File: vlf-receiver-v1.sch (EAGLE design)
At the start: 46 parts, among them P10 10k, Q1 BC237A/EQUIV, Q2 BC237A/EQUIV, U1 MC7809, U2 TLE2426, U3 LM386

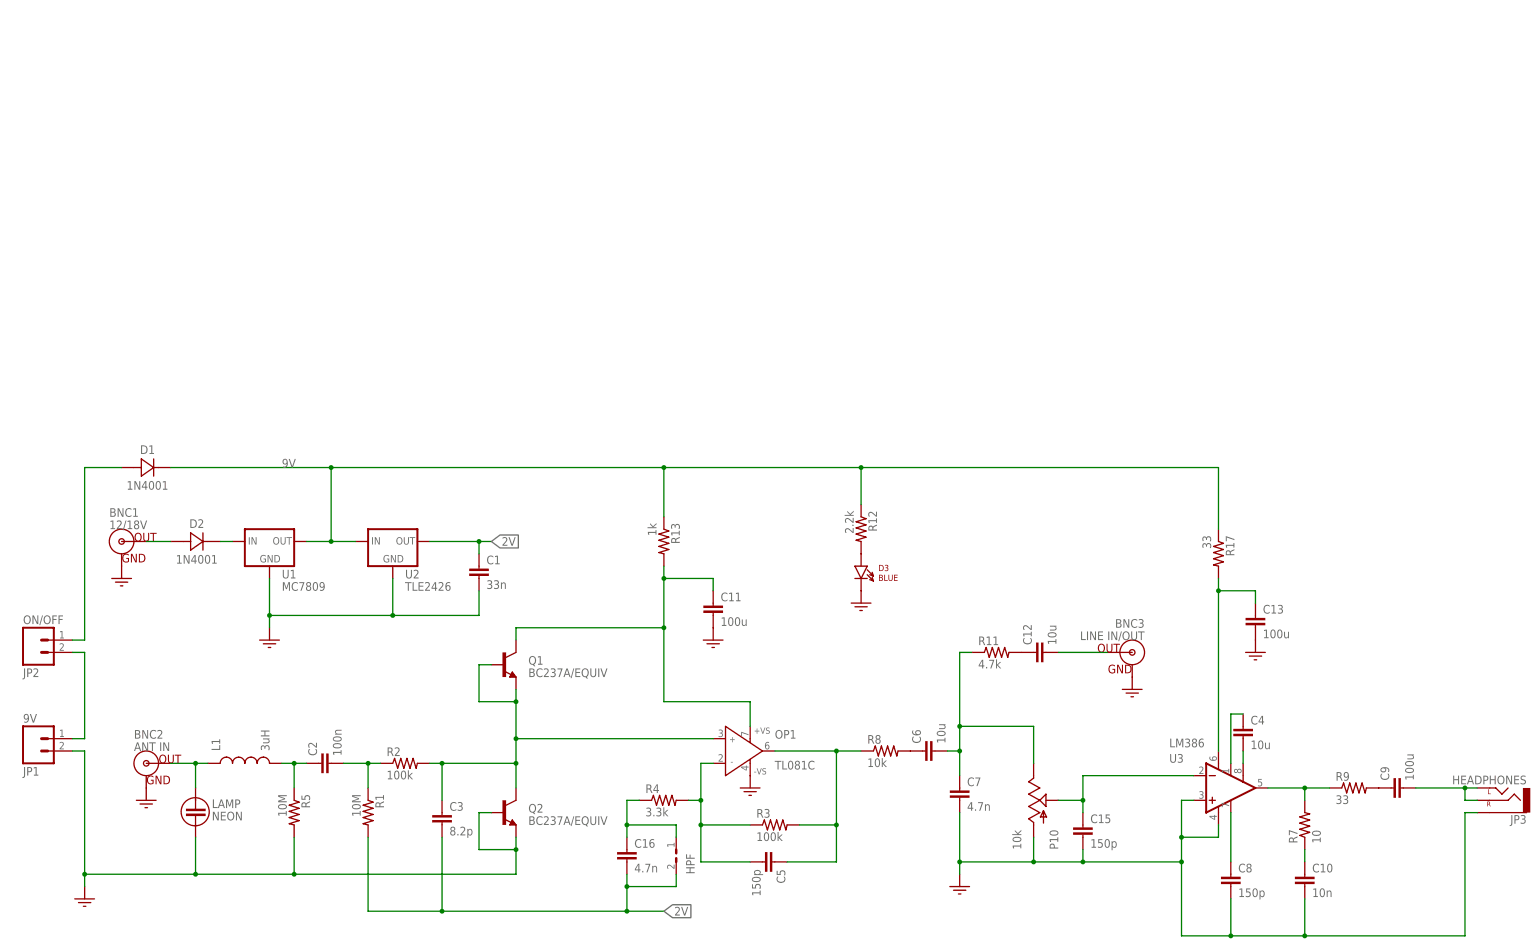
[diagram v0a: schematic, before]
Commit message: Changed name. Cleaned up schematic. Added notes and exported BOM. Need to compare.
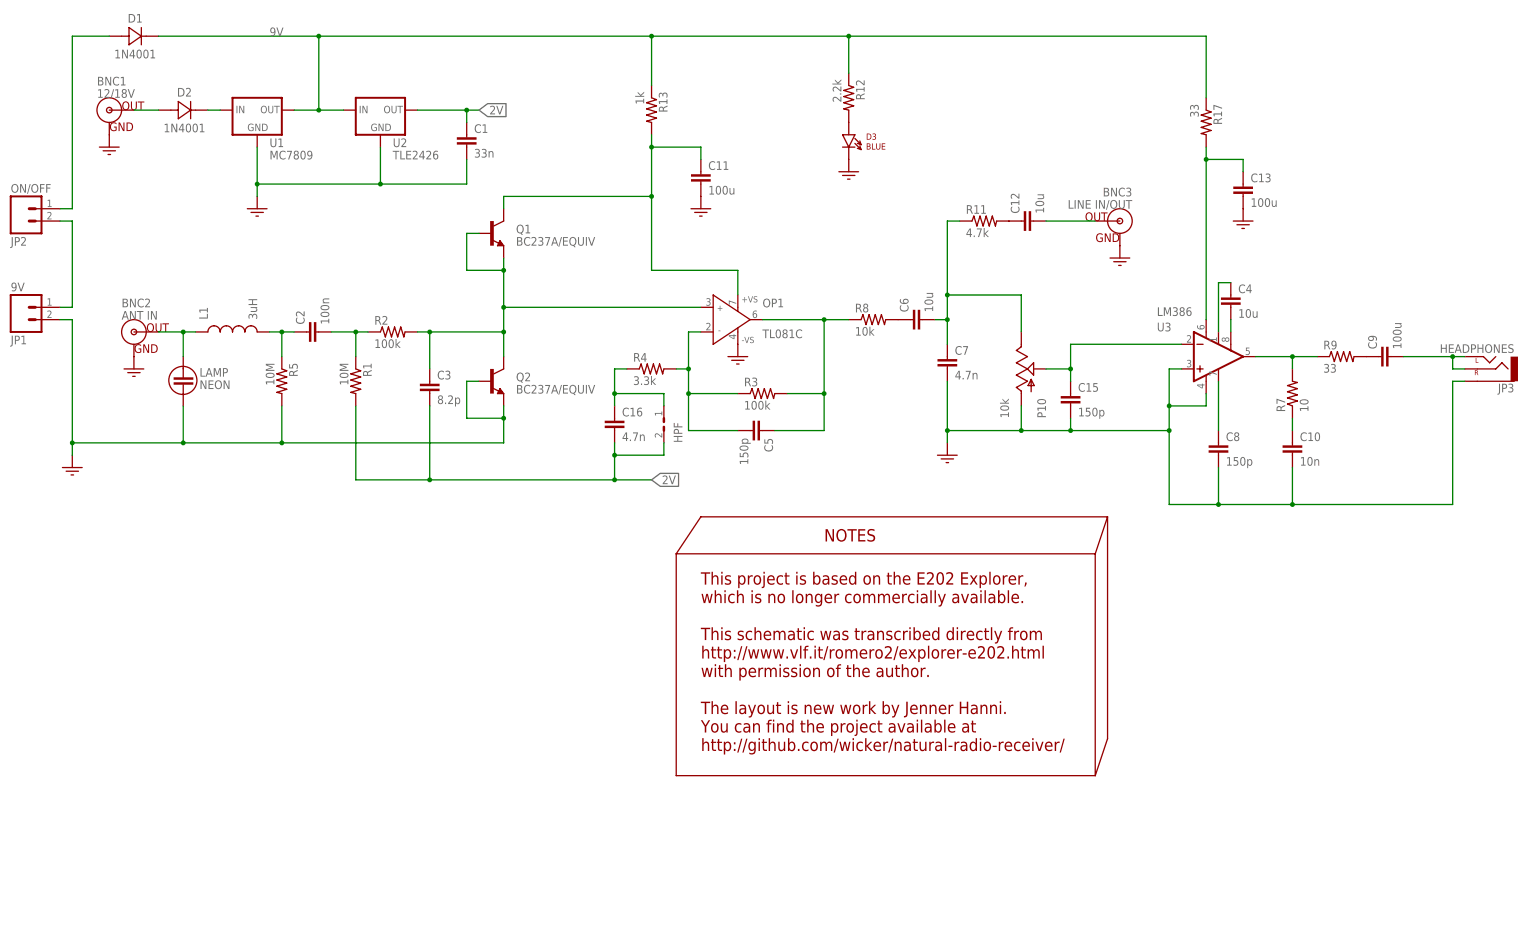
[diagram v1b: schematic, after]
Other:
- note added: "NOTES"
- note added: "This project is based on the E202 Explorer, which is no longer commercially available. This schematic was transcribed directly from http://www.vlf.it/romero2/explorer-e202.html with permission of the author. The layout is new work by Jenner Hanni. You can find the project available at http://github.com/wicker/natural-radio-receiver/"
- moved on the sheet: BNC1, BNC2, BNC3, C1, C10, C11, C12, C13, C15, C16, C2, C3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
